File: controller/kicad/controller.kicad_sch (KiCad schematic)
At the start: 40 parts, among them J1 pcie_98, J2 USB_C_Receptacle_USB2.0, SW2 D2F-01F-A, U1 WeAct_STM32H750_Module, U10 ESD5344D, U11 ESD5344D, U12 ESD5344D, U13 ESD5344D, U14 ESD5344D, U15 ESD5344D, U16 CP2102N-A02-GQFN28R, U17 ESD5344D, U2 ESD5344D, U3 ESD5344D, U4 ESD5344D, U5 ESD5344D, U6 ESD5344D, U7 ESD5344D, U8 ESD5344D, U9 ESD5344D

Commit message: Minor tweak of the schematics.
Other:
- note added: "ESD Protection"
- note removed: "ESD Projection"
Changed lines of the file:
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@@
     (stroke (width 0) (type default))
   )
-  (text "ESD Projection" (at 95.25 254.635 0)
+  (text "ESD Protection" (at 95.25 254.635 0)
     (effects (font (size 3 3) (thickness 0.6) bold) (justify left bottom))
   )

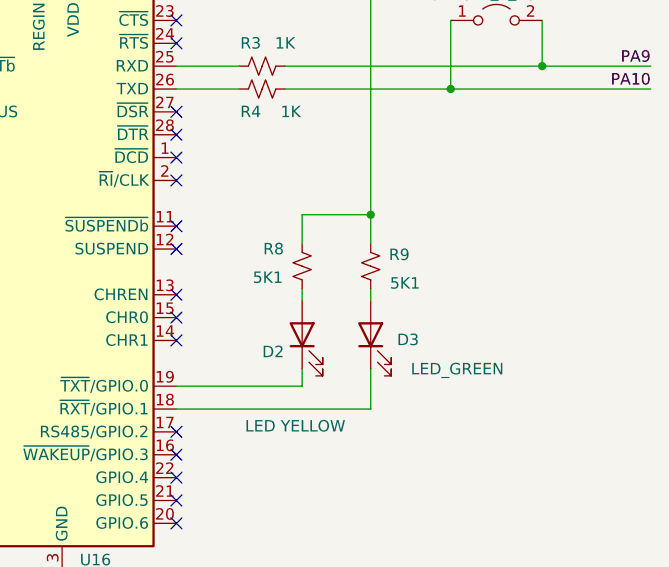
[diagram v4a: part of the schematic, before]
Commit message: Increased the series resistor of the controller's green led from 5k to 10k.
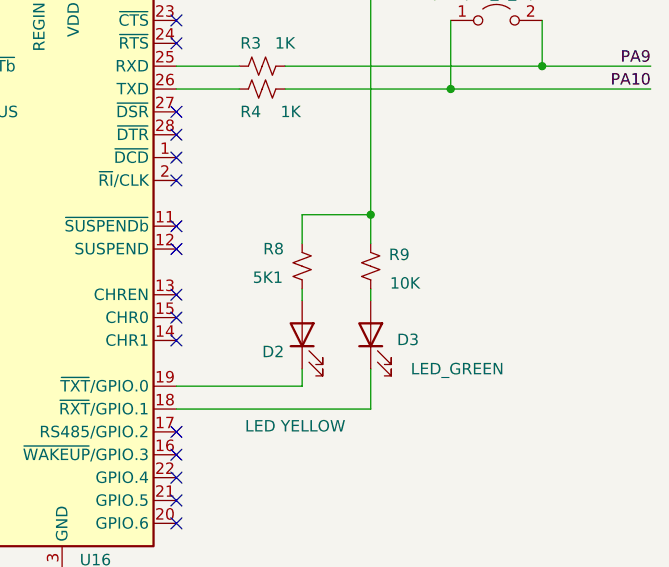
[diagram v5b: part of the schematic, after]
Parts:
- R9: value 5K1 -> 10K; LCSC C23186 -> C25744
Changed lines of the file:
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@@
       (effects (font (size 1.27 1.27)))
     )
-    (property "Value" "5K1" (at 354.33 203.2 0)
+    (property "Value" "10K" (at 354.33 203.2 0)
       (effects (font (size 1.27 1.27)))
     )
@@
       (effects (font (size 1.27 1.27)) hide)
     )
-    (property "LCSC" "C23186" (at 350.52 201.295 0)
+    (property "LCSC" "C25744" (at 350.52 201.295 0)
       (effects (font (size 1.27 1.27)) hide)
     )

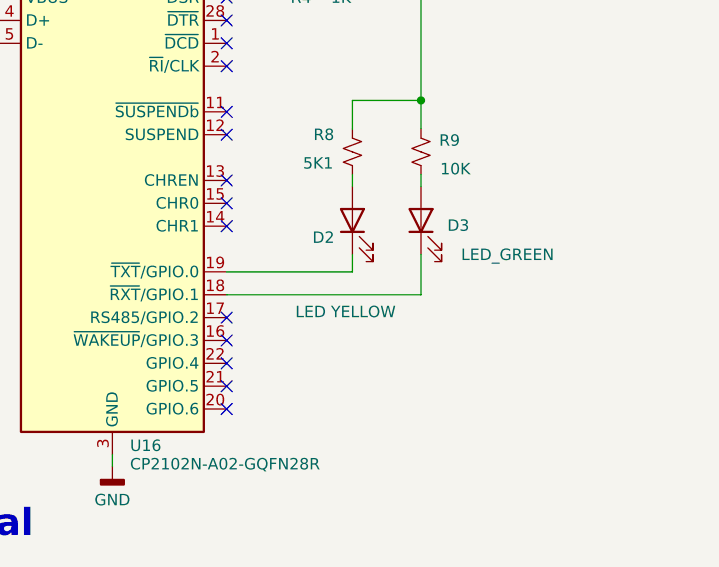
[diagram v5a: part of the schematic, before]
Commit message: Tweaked LEDs values.
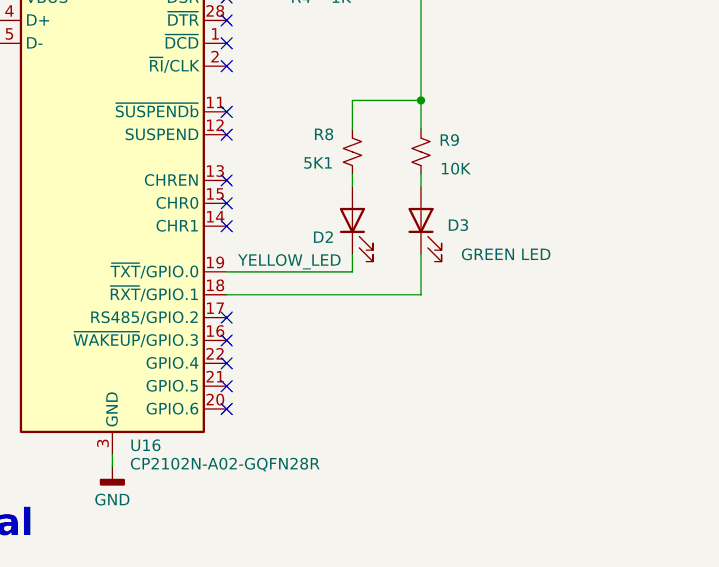
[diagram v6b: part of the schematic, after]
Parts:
- D2: value LED YELLOW -> YELLOW_LED
- D3: value LED_GREEN -> GREEN LED
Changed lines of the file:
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@@
       (effects (font (size 1.27 1.27)) (justify right))
     )
-    (property "Value" "LED YELLOW" (at 336.55 219.075 90)
+    (property "Value" "YELLOW_LED" (at 330.2 213.36 90)
       (effects (font (size 1.27 1.27)) (justify right))
     )
@@
       (effects (font (size 1.27 1.27)) (justify right))
     )
-    (property "Value" "LED_GREEN" (at 354.965 212.725 90)
+    (property "Value" "GREEN LED" (at 354.965 212.725 90)
       (effects (font (size 1.27 1.27)) (justify right))
     )

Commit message: Generated JLCPCB production files.
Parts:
- JP1: footprint Connector_PinHeader_2.54mm:PinHeader_1x02_P2.54mm_Vertical -> controller:PinHeader_1x02_P2.54mm_Vertical
- U16: JLCRotOffset (none) -> 90
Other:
- title: (none) -> Controller
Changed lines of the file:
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@@
 (kicad_sch (version 20230121) (generator eeschema)
   (paper "A3")
+  (title_block
+    (title "Controller")
+    (rev "0.2")
+  )
   (junction (at 104.775 43.18) (diameter 0) (color 0 0 0 0)
   )
@@
       (effects (font (size 1.27 1.27)))
     )
-    (property "Footprint" "Connector_PinHeader_2.54mm:PinHeader_1x02_P2.54mm_Vertical" (at 364.49 173.99 0)
+    (property "Footprint" "controller:PinHeader_1x02_P2.54mm_Vertical" (at 364.49 173.99 0)
       (effects (font (size 1.27 1.27)) hide)
     )
@@
       (effects (font (size 1.27 1.27)) hide)
     )
+    (property "JLCRotOffset" "90" (at 316.23 201.93 0)
+      (effects (font (size 1.27 1.27)) hide)
+    )

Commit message: Fixed the JLC part number of Controller's R9 (was 0402, should be 0603 10K).
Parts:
- R9: LCSC C25744 -> C25804
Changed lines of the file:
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@@
       (effects (font (size 1.27 1.27)) hide)
     )
-    (property "LCSC" "C25744" (at 350.52 201.295 0)
+    (property "LCSC" "C25804" (at 350.52 201.295 0)
       (effects (font (size 1.27 1.27)) hide)
     )
